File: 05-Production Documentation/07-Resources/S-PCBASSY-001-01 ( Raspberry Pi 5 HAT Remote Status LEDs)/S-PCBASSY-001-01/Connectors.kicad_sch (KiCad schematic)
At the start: 18 parts, among them Q1 BSS138, Q2 BSS138, Q3 BSS138

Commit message: WIP - LED Driver and Started with Connectors
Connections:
- net LED_CATHODE_ERROR: now also Rg5.2; no longer D6.1 (K), Q3.3 (D)
- net LED_CATHODE_MEDIA: now also Rg6.2; no longer D5.1 (K), Q1.3 (D)
- net LED_CATHODE_POWER: now also Rg4.2; no longer D4.1 (K), Q2.3 (D)
- net at Rg4.1: now also D4.1 (K), Q2.3 (D)
- net at Rg5.1: now also D6.1 (K), Q3.3 (D)
- net at Rg6.1: now also D5.1 (K), Q1.3 (D)
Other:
- moved on the sheet: D2, D3, D4, D5, D6, Q2, Q3, Rg2, Rg3, Rg4, Rg5, Rg6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

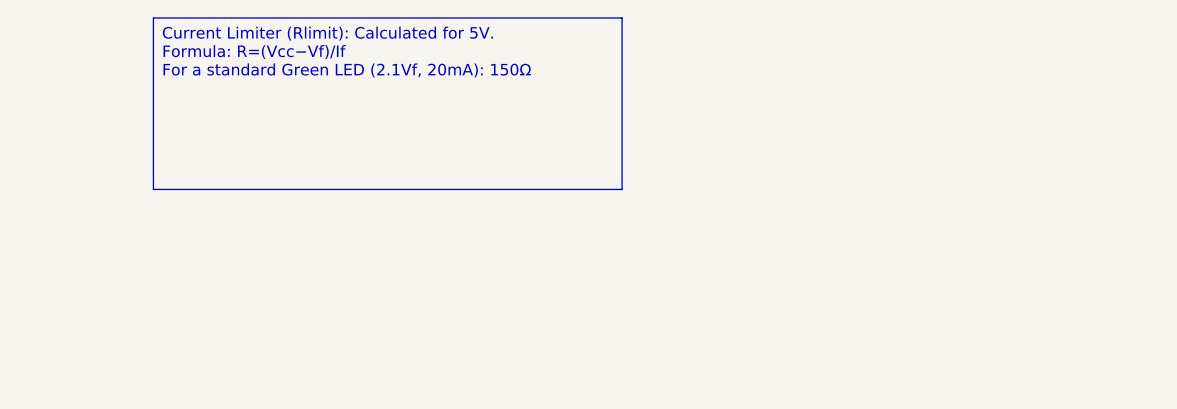
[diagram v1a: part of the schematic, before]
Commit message: Rpi Filetring and protection added
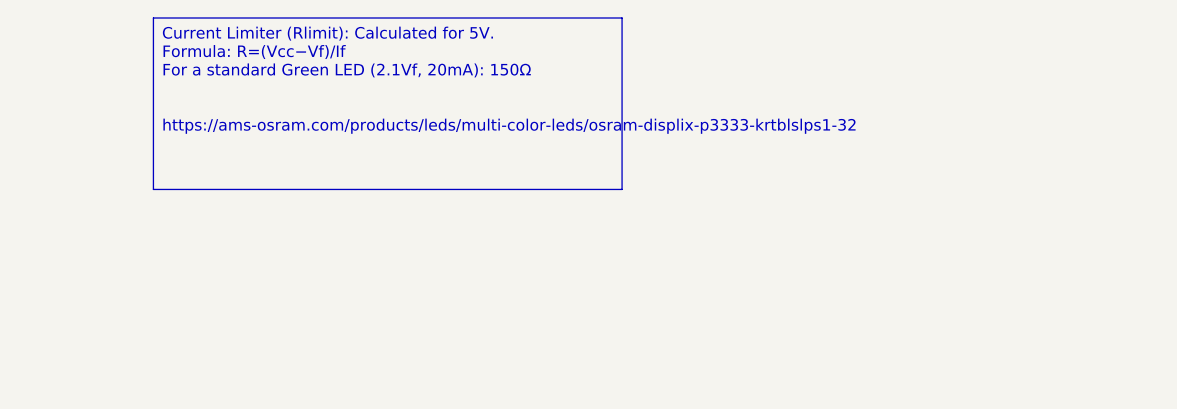
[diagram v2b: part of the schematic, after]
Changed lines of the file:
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@@
 	(generator_version "9.0")
 	(paper "A4")
-	(text_box "Current Limiter (Rlimit​): Calculated for 5V.\n    Formula: R=(Vcc​−Vf​)/If​\n    For a standard Green LED (2.1Vf​, 20mA): 150Ω"
+	(text_box "Current Limiter (Rlimit​): Calculated for 5V.\n    Formula: R=(Vcc​−Vf​)/If​\n    For a standard Green LED (2.1Vf​, 20mA): 150Ω\n\n\nhttps://ams-osram.com/products/leds/multi-color-leds/osram-displix-p3333-krtblslps1-32"
 		(exclude_from_sim no)
 		(at 175.26 17.78 0)

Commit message: Schematics done
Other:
- note added: "Blue LED Driver"
- note added: "Green LED Driver"
- note added: "Notes"
- note added: "RED LED Driver"
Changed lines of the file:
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@@
 	(generator_version "9.0")
 	(paper "A4")
+	(rectangle
+		(start 17.78 74.93)
+		(end 115.57 121.92)
+		(stroke
+			(width 0)
+			(type dash_dot)
+		)
+		(fill
+			(type none)
+		)
+	)
+	(rectangle
+		(start 17.78 132.08)
+		(end 115.57 179.07)
+		(stroke
+			(width 0)
+			(type dash_dot)
+		)
+		(fill
+			(type none)
+		)
+	)
+	(rectangle
+		(start 17.78 20.32)
+		(end 115.57 67.31)
+		(stroke
+			(width 0)
+			(type dash_dot)
+		)
+		(fill
+			(type none)
+		)
+	)
+	(text "Notes\n"
+		(exclude_from_sim no)
+		(at 185.928 16.002 0)
+		(effects
+			(font
+				(size 2.286 2.286)
+			)
+		)
+	)
+	(text "RED LED Driver"
+		(exclude_from_sim no)
+		(at 18.288 129.286 0)
+		(effects
+			(font
+				(size 2.286 2.286)
+			)
+			(justify left)
+		)
+	)
+	(text "Green LED Driver"
+		(exclude_from_sim no)
+		(at 18.288 72.136 0)
+		(effects
+			(font
+				(size 2.286 2.286)
+			)
+			(justify left)
+		)
+	)
+	(text "Blue LED Driver"
+		(exclude_from_sim no)
+		(at 18.288 17.526 0)
+		(effects
+			(font
+				(size 2.286 2.286)
+			)
+			(justify left)
+		)
+	)
 	(text_box "Current Limiter (Rlimit​): Calculated for 5V.\n    Formula: R=(Vcc​−Vf​)/If​\n    For a standard Green LED (2.1Vf​, 20mA): 150Ω\n\n\nhttps://ams-osram.com/products/leds/multi-color-leds/osram-displix-p3333-krtblslps1-32"
 		(exclude_from_sim no)
-		(at 175.26 17.78 0)
-		(size 52.07 19.05)
+		(at 181.61 17.78 0)
+		(size 96.52 19.05)
 		(margins 0.9525 0.9525 0.9525 0.9525)
 		(stroke
@@
 		)
 		(fill
-			(type none)
+			(type color)
+			(color 255 255 194 1)
 		)
 		(effects
@@
 			(table_cell "LED Color"
 				(exclude_from_sim no)
-				(at 173.99 39.37 0)
+				(at 181.61 38.1 0)
 				(size 20.32 2.54)
 				(margins 0.9525 0.9525 0.9525 0.9525)
@@
 			(table_cell "Typical Vf​"
 				(exclude_from_sim no)
-				(at 194.31 39.37 0)
+				(at 201.93 38.1 0)
 				(size 20.32 2.54)
 				(margins 0.9525 0.9525 0.9525 0.9525)
@@
 			(table_cell "Calculation"
 				(exclude_from_sim no)
-				(at 214.63 39.37 0)
+				(at 222.25 38.1 0)
 				(size 20.32 2.54)
 				(margins 0.9525 0.9525 0.9525 0.9525)
@@
 			(table_cell "Calculated R"
 				(exclude_from_sim no)
-				(at 234.95 39.37 0)
+				(at 242.57 38.1 0)
 				(size 20.32 2.54)
 				(margins 0.9525 0.9525 0.9525 0.9525)
@@
 			(table_cell "Standard Resistor"
 				(exclude_from_sim no)
-				(at 255.27 39.37 0)
+				(at 262.89 38.1 0)
 				(size 20.32 2.54)
 				(margins 0.9525 0.9525 0.9525 0.9525)
@@
 			(table_cell "RED (Error)"
 				(exclude_from_sim no)
-				(at 173.99 41.91 0)
+				(at 181.61 40.64 0)
 				(size 20.32 2.54)
 				(margins 0.9525 0.9525 0.9525 0.9525)
@@
 			(table_cell "2.0V"
 				(exclude_from_sim no)
-				(at 194.31 41.91 0)
+				(at 201.93 40.64 0)
 				(size 20.32 2.54)
 				(margins 0.9525 0.9525 0.9525 0.9525)
@@
 			(table_cell "(5−2.0)/0.02"
 				(exclude_from_sim no)
-				(at 214.63 41.91 0)
+				(at 222.25 40.64 0)
 				(size 20.32 2.54)
 				(margins 0.9525 0.9525 0.9525 0.9525)
@@
 			(table_cell "150Ω"
 				(exclude_from_sim no)
-				(at 234.95 41.91 0)
+				(at 242.57 40.64 0)
 				(size 20.32 2.54)
 				(margins 0.9525 0.9525 0.9525 0.9525)
@@
 			(table_cell "150Ω"
 				(exclude_from_sim no)
-				(at 255.27 41.91 0)
+				(at 262.89 40.64 0)
 				(size 20.32 2.54)
 				(margins 0.9525 0.9525 0.9525 0.9525)
@@
 			(table_cell "GREEN (Media)"
 				(exclude_from_sim no)
-				(at 173.99 44.45 0)
+				(at 181.61 43.18 0)
 				(size 20.32 2.54)
 				(margins 0.9525 0.9525 0.9525 0.9525)
@@
 			(table_cell "2.1V"
 				(exclude_from_sim no)
-				(at 194.31 44.45 0)
+				(at 201.93 43.18 0)
 				(size 20.32 2.54)
 				(margins 0.9525 0.9525 0.9525 0.9525)
@@
 			(table_cell "(5−2.1)/0.02"
 				(exclude_from_sim no)
-				(at 214.63 44.45 0)
+				(at 222.25 43.18 0)
 				(size 20.32 2.54)
 				(margins 0.9525 0.9525 0.9525 0.9525)
@@
 			(table_cell "145Ω"
 				(exclude_from_sim no)
-				(at 234.95 44.45 0)
+				(at 242.57 43.18 0)
 				(size 20.32 2.54)
 				(margins 0.9525 0.9525 0.9525 0.9525)
@@
 			(table_cell "150Ω"
 				(exclude_from_sim no)
-				(at 255.27 44.45 0)
+				(at 262.89 43.18 0)
 				(size 20.32 2.54)
 				(margins 0.9525 0.9525 0.9525 0.9525)
@@
 			(table_cell "BLUE (Power)"
 				(exclude_from_sim no)
-				(at 173.99 46.99 0)
+				(at 181.61 45.72 0)
 				(size 20.32 2.54)
 				(margins 0.9525 0.9525 0.9525 0.9525)
@@
 			(table_cell "3.2V"
 				(exclude_from_sim no)
-				(at 194.31 46.99 0)
+				(at 201.93 45.72 0)
 				(size 20.32 2.54)
 				(margins 0.9525 0.9525 0.9525 0.9525)
@@
 			(table_cell "(5−3.2)/0.02"
 				(exclude_from_sim no)
-				(at 214.63 46.99 0)
+				(at 222.25 45.72 0)
 				(size 20.32 2.54)
 				(margins 0.9525 0.9525 0.9525 0.9525)
@@
 			(table_cell "90Ω"
 				(exclude_from_sim no)
-				(at 234.95 46.99 0)
+				(at 242.57 45.72 0)
 				(size 20.32 2.54)
 				(margins 0.9525 0.9525 0.9525 0.9525)
@@
 			(table_cell "91Ω or 100Ω"
 				(exclude_from_sim no)
-				(at 255.27 46.99 0)
+				(at 262.89 45.72 0)
 				(size 20.32 2.54)
 				(margins 0.9525 0.9525 0.9525 0.9525)
@@
 			(table_cell ""
 				(exclude_from_sim no)
-				(at 173.99 49.53 0)
+				(at 181.61 48.26 0)
 				(size 20.32 2.54)
 				(margins 0.9525 0.9525 0.9525 0.9525)
@@
 			(table_cell ""
 				(exclude_from_sim no)
-				(at 194.31 49.53 0)
+				(at 201.93 48.26 0)
 				(size 20.32 2.54)
 				(margins 0.9525 0.9525 0.9525 0.9525)
@@
 			(table_cell ""
 				(exclude_from_sim no)
-				(at 214.63 49.53 0)
+				(at 222.25 48.26 0)
 				(size 20.32 2.54)
 				(margins 0.9525 0.9525 0.9525 0.9525)
@@
 			(table_cell ""
 				(exclude_from_sim no)
-				(at 234.95 49.53 0)
+				(at 242.57 48.26 0)
 				(size 20.32 2.54)
 				(margins 0.9525 0.9525 0.9525 0.9525)
@@
 			(table_cell ""
 				(exclude_from_sim no)
-				(at 255.27 49.53 0)
+				(at 262.89 48.26 0)
 				(size 20.32 2.54)
 				(margins 0.9525 0.9525 0.9525 0.9525)
@@
 			(table_cell ""
 				(exclude_from_sim no)
-				(at 173.99 52.07 0)
+				(at 181.61 50.8 0)
 				(size 20.32 2.54)
 				(margins 0.9525 0.9525 0.9525 0.9525)
@@
 			(table_cell ""
 				(exclude_from_sim no)
-				(at 194.31 52.07 0)
+				(at 201.93 50.8 0)
 				(size 20.32 2.54)
 				(margins 0.9525 0.9525 0.9525 0.9525)
@@
 			(table_cell ""
 				(exclude_from_sim no)
-				(at 214.63 52.07 0)
+				(at 222.25 50.8 0)
 				(size 20.32 2.54)
 				(margins 0.9525 0.9525 0.9525 0.9525)
@@
 			(table_cell ""
 				(exclude_from_sim no)
-				(at 234.95 52.07 0)
+				(at 242.57 50.8 0)
 				(size 20.32 2.54)
 				(margins 0.9525 0.9525 0.9525 0.9525)
@@
 			(table_cell ""
 				(exclude_from_sim no)
-				(at 255.27 52.07 0)
-				(size 20.32 2.54)
-				(margins 0.9525 0.9525 0.9525 0.9525)
+				(at 262.89 50.8 0)
+				(size 20.32 2.54)
+				(margins 0.9525 0.9525 0.9525 0.9525)

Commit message: Imported Components to PCB
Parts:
- Rg1, Rg2, Rg4, Rg5, Rg6, Rpd1, Rpd2, Rpd3: footprint (none) -> Capacitor_SMD:C_0603_1608Metric
- Rg3: footprint (none) -> Resistor_SMD:R_0603_1608Metric_Pad0.98x0.95mm_HandSolder
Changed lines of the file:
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@@
 			)
 		)
-		(property "Footprint" ""
+		(property "Footprint" "Capacitor_SMD:C_0603_1608Metric"
 			(at 80.518 29.21 90)
 			(effects
@@
 			)
 		)
-		(property "Footprint" ""
+		(property "Footprint" "Capacitor_SMD:C_0603_1608Metric"
 			(at 84.328 139.7 90)
 			(effects
@@
 			)
 		)
-		(property "Footprint" ""
+		(property "Footprint" "Capacitor_SMD:C_0603_1608Metric"
 			(at 84.328 83.82 90)
 			(effects
@@
 			)
 		)
-		(property "Footprint" ""
+		(property "Footprint" "Capacitor_SMD:C_0603_1608Metric"
 			(at 48.26 99.568 90)
 			(effects
@@
 			)
 		)
-		(property "Footprint" ""
+		(property "Footprint" "Resistor_SMD:R_0603_1608Metric_Pad0.98x0.95mm_HandSolder"
 			(at 48.26 155.448 90)
 			(effects
@@
 			)
 		)
-		(property "Footprint" ""
+		(property "Footprint" "Capacitor_SMD:C_0603_1608Metric"
 			(at 57.658 104.14 90)
 			(effects
@@
 			)
 		)
-		(property "Footprint" ""
+		(property "Footprint" "Capacitor_SMD:C_0603_1608Metric"
 			(at 53.848 49.53 90)
 			(effects
@@
 			)
 		)
-		(property "Footprint" ""
+		(property "Footprint" "Capacitor_SMD:C_0603_1608Metric"
 			(at 57.658 160.02 90)
 			(effects
@@
 			)
 		)
-		(property "Footprint" ""
+		(property "Footprint" "Capacitor_SMD:C_0603_1608Metric"
 			(at 44.45 44.958 90)
 			(effects
